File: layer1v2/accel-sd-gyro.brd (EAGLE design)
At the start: 17 parts, among them IC2 LGD20H, U1 MMA8452Q, U2 microSD

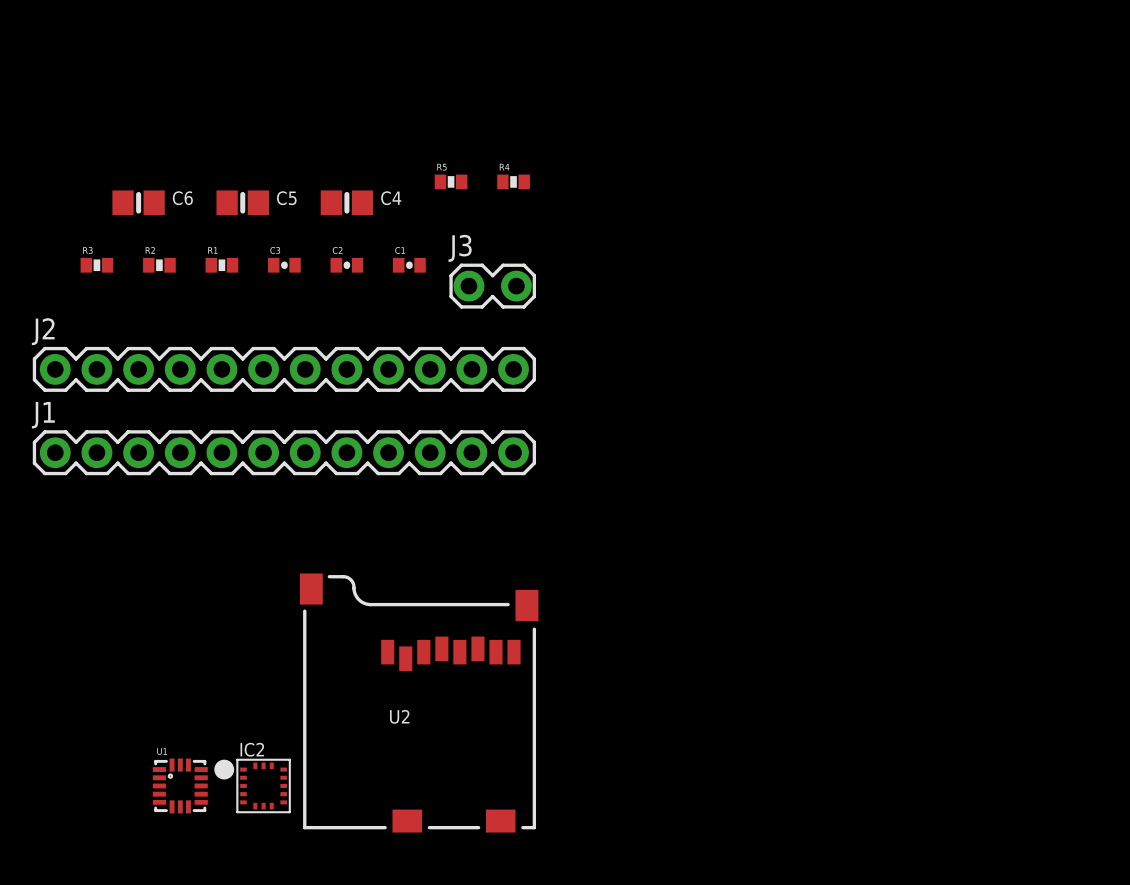
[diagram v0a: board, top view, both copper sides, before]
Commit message: created layout for just the gyro
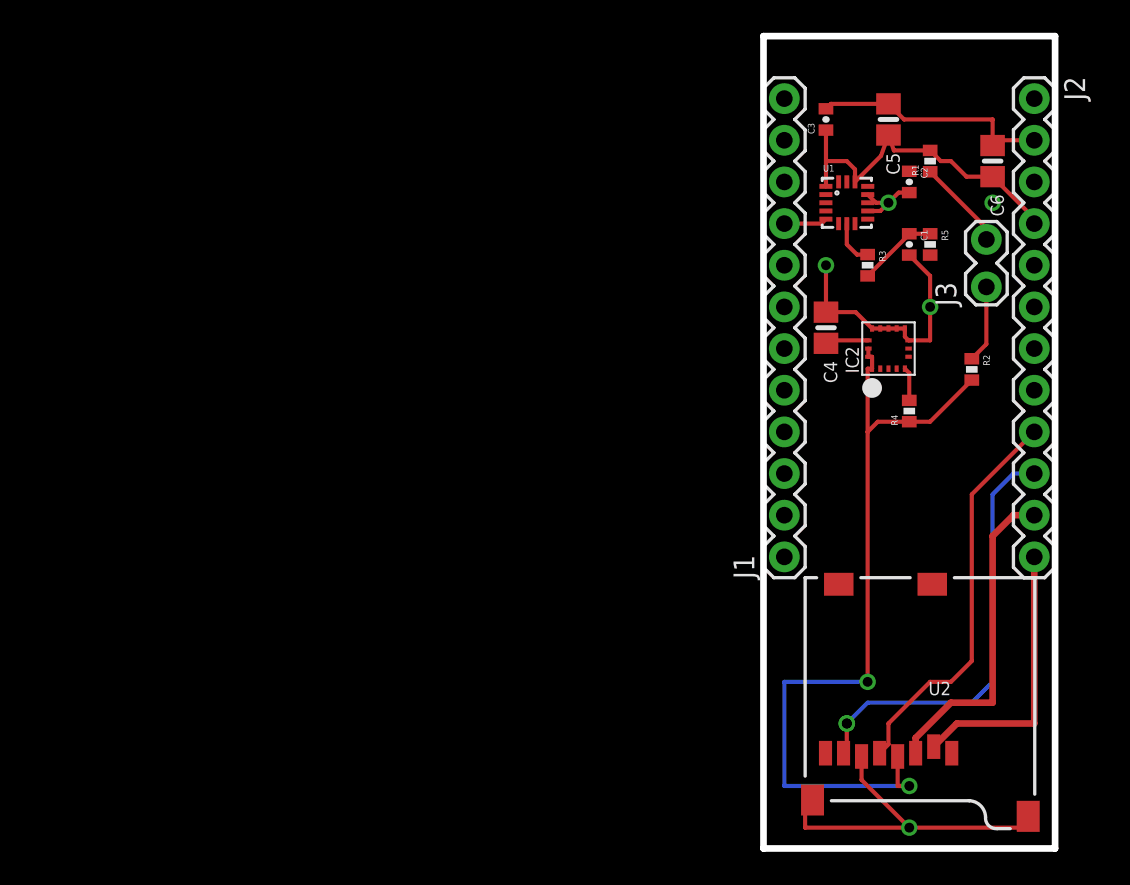
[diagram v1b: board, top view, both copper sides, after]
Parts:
- moved J2 61.9 mm to (16.5, 45.7), turned to 270 degrees
- moved U1 54.0 mm to (5.08, 39.4)
- moved C6 52.1 mm to (14.0, 41.9), turned to 270 degrees
- moved R2 49.9 mm to (12.7, 29.2), turned to 270 degrees
- moved R3 47.0 mm to (6.35, 35.6), turned to 270 degrees
- moved IC2 46.5 mm to (7.62, 30.5), turned to 90 degrees
- moved J1 44.9 mm to (1.27, 17.8), turned to 90 degrees
- moved R1 43.6 mm to (10.2, 41.9), turned to 90 degrees
- moved C5 39.7 mm to (7.62, 44.5), turned to 270 degrees
- moved C2 34.7 mm to (8.89, 40.6), turned to 270 degrees
- moved C3 34.2 mm to (3.81, 44.5), turned to 90 degrees
- moved J3 31.4 mm to (13.6, 34.4), turned to 90 degrees
- moved C1 30.5 mm to (8.89, 36.8), turned to 270 degrees
- moved C4 30.2 mm to (3.81, 31.8), turned to 270 degrees
- moved R5 29.5 mm to (10.2, 36.8), turned to 270 degrees
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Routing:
- net 3.3V: track 0.00 -> 76.3 mm, vias 0 -> 2
- net GND: track 0.00 -> 60.2 mm, vias 0 -> 3
- net MISO: track 0.00 -> 26.3 mm, vias 0 -> 1
- net SCK: track 0.00 -> 24.2 mm
- net MOSI: track 0.00 -> 19.7 mm
- net SD_CS: track 0.00 -> 16.9 mm
- net SCL: track 0.00 -> 5.55 mm
- net SDA: track 0.00 -> 4.75 mm
- net SA0: track 0.00 -> 2.79 mm
- net N$3: track 0.00 -> 2.66 mm
- net CS_3.3V: track 0.00 -> 2.05 mm
- added copper zone on layer 16, net GND
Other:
- board outline added: 17.8 x 49.5 mm

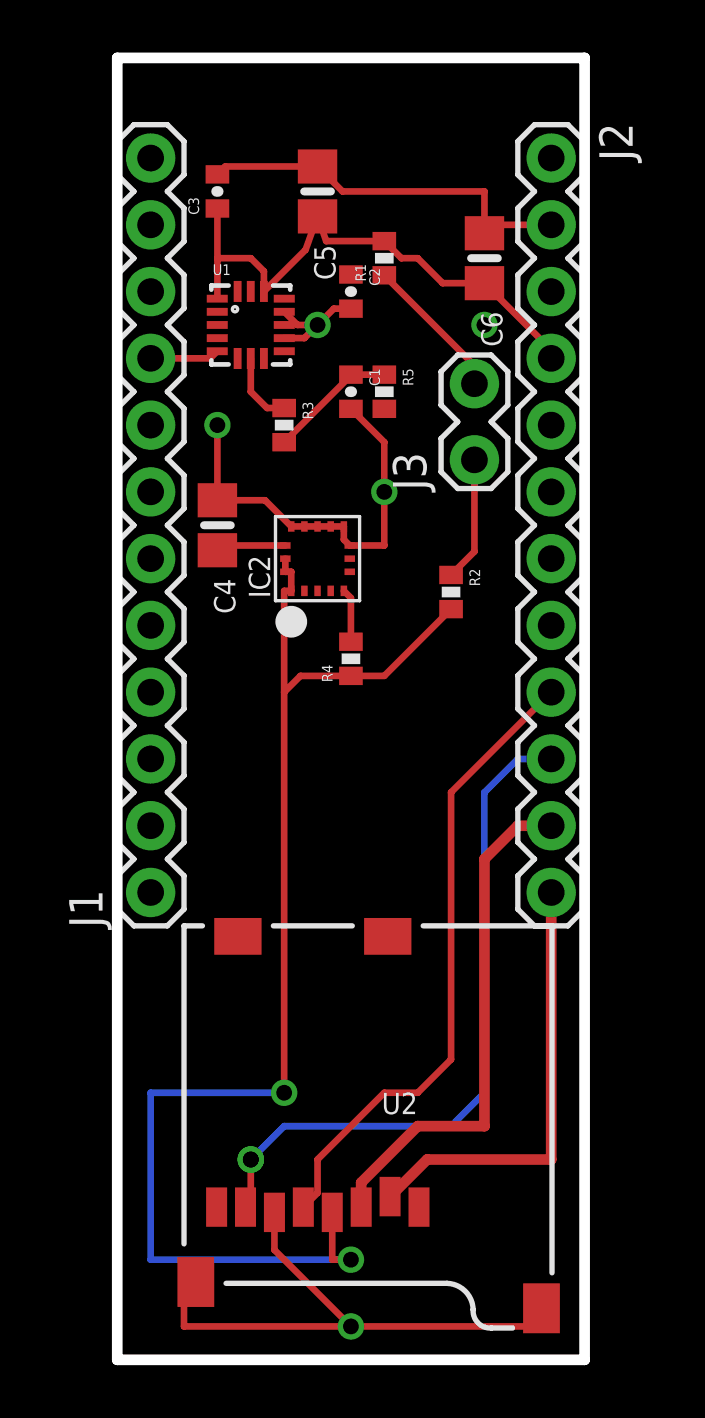
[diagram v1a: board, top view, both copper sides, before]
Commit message: intial layout of v2 board, consldated i2c resisor, added header pin row
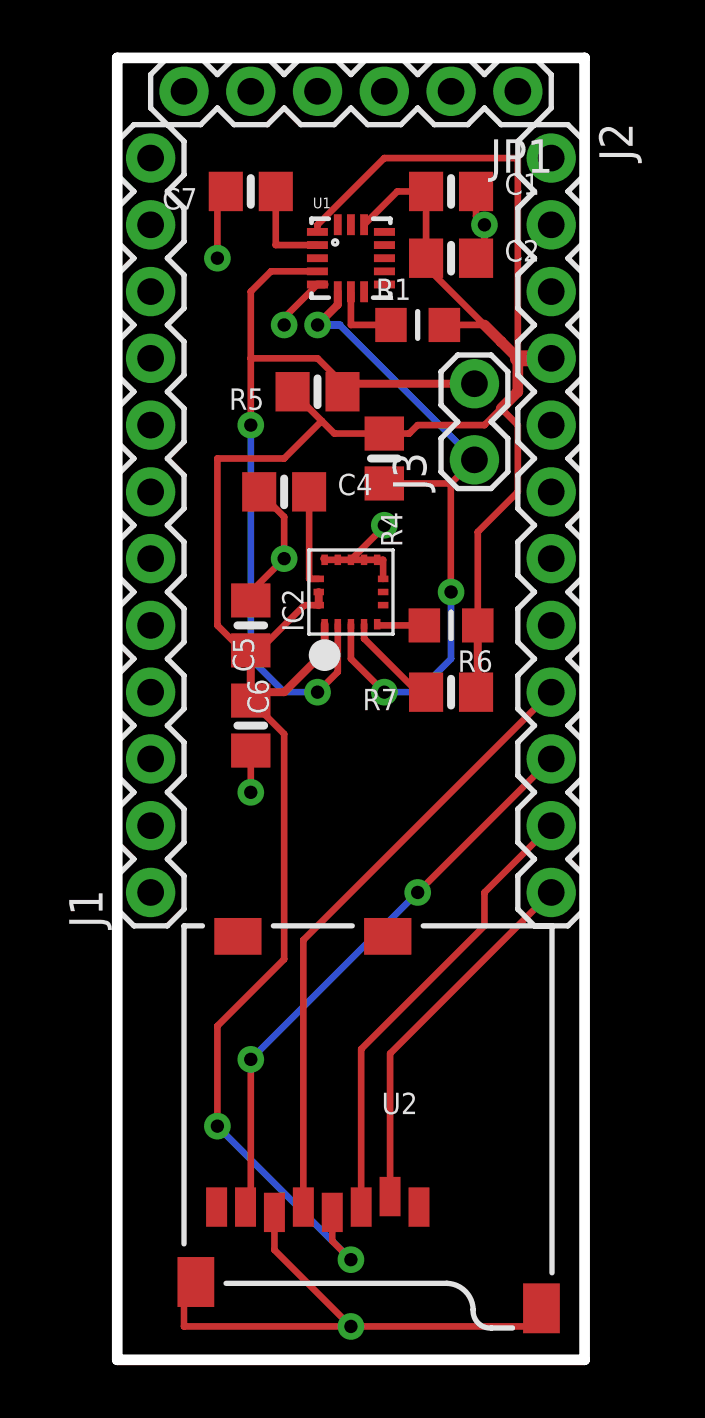
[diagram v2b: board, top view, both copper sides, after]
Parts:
- removed C3: 4.7uF, SparkFun:0402-CAP
- removed R2, R3: 10k, SparkFun:0402-RES
- added C7: 0.1uF, microbuilder:0805-NO
- added JP1: FTDI Basic, SparkFun:1X06
- added R6: 10K, microbuilder:_0805MP
- added R7: 10K, microbuilder:0805-NO
- C1: device SparkFun:0402-CAP -> microbuilder:0805-NO
- C2: value 0.1uF -> 4.7uF; device SparkFun:0402-CAP -> microbuilder:0805-NO
- R1: value 10k -> 10K; device SparkFun:0402-RES -> microbuilder:_0805MP
- R4, R5: value 10k -> 10K; device SparkFun:0402-RES -> microbuilder:0805-NO
- moved C5 20.5 mm to (5.08, 24.1), turned to 90 degrees
- moved C6 16.6 mm to (5.08, 27.9)
- moved C1 8.52 mm to (12.7, 44.5), turned to 0 degrees
- moved R4 7.73 mm to (10.2, 34.3), turned to 270 degrees
- moved U1 4.58 mm to (8.89, 41.9)
- moved C2 4.02 mm to (12.7, 41.9), turned to 0 degrees
- moved C4 2.84 mm to (6.35, 33.0), turned to 0 degrees
- moved R1 2.84 mm to (11.4, 39.4), turned to 0 degrees
- moved R5 2.54 mm to (7.62, 36.8), turned to 180 degrees
- moved IC2 1.80 mm to (8.89, 29.2)
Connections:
- removed net 3.3V: C1.1, C3.1, C5.2, C6.2, IC2.1, IC2.15, IC2.16, J2.4, R1.2, R2.2, R3.2, R4.1, R5.1, U1.1, U1.14, U2.4
- new net +3V3: C1.1, C2.1, C5.2, C6.2, IC2.1, IC2.15, IC2.16, J2.4, JP1.4, R1.2, R4.1, R5.2, R6.1, R7.1, U1.1, U1.14, U2.4
- new net DTR: JP1.1
- new net RXI: JP1.3
- new net TXO: JP1.2
- net BYP: now also C7.1; no longer C2.1
- net CS_3.3V: now also R6.2; no longer R4.2
- net GND: now also C7.2, JP1.5, JP1.6; no longer C3.2
- net SA0: now also R1.1; no longer R3.1
- net SCL: now also R5.1; no longer R1.1
- net SDA: now also R4.2; no longer R2.1
- net SDO/SAO: now also R7.2; no longer R5.2
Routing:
- net +3V3: track 0.00 -> 104.0 mm, vias 0 -> 2
- net 3.3V: track 76.3 -> 0.00 mm, vias 2 -> 0
- net SCL: track 5.55 -> 32.6 mm, vias 0 -> 2
- net SDA: track 4.75 -> 26.3 mm, vias 0 -> 3
- net GND: track 60.2 -> 41.5 mm, vias 3 -> 6
- net MISO: track 26.3 -> 22.0 mm, vias 1 -> 2
- net SDO/SAO: track 0.00 -> 4.20 mm
- net BYP: track 0.00 -> 3.63 mm
- net SD_CS: track 16.9 -> 14.1 mm
- net MOSI: track 19.7 -> 17.5 mm
- net N$3: track 2.66 -> 3.68 mm
- net SCK: track 24.2 -> 23.5 mm

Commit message: layer 1 tweaks and silk
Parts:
- removed JP1: FTDI Basic, SparkFun:1X06
- removed R6: 10K, microbuilder:_0805MP
- removed R7: 10K, microbuilder:0805-NO
- added R2: 10K, microbuilder:0805-NO
- added R3: 10K, microbuilder:_0805MP
- R1: device microbuilder:_0805MP -> microbuilder:0805-NO
- R4: device microbuilder:0805-NO -> microbuilder:_0805MP
- moved R5 12.0 mm to (11.4, 25.4)
- moved R4 6.84 mm to (12.7, 27.9), turned to 180 degrees
- moved R1 4.58 mm to (7.62, 36.8), turned to 180 degrees
- moved C2 1.27 mm to (14.0, 41.9), turned to 270 degrees
- moved C1 1.27 mm to (11.4, 44.5)
- renumbered C7 to C3
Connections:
- removed net DTR: JP1.1
- removed net RXI: JP1.3
- removed net TXO: JP1.2
- net +3V3: now also R2.1, R3.2, R5.1; no longer JP1.4, R5.2, R6.1, R7.1
- net CS_3.3V: now also R4.2; no longer R6.2
- net GND: no longer JP1.5, JP1.6
- net SA0: now also R3.1; no longer R1.1
- net SCL: now also R1.1; no longer R5.1
- net SDA: now also R2.2; no longer R4.2
- net SDO/SAO: now also R5.2; no longer R7.2
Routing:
- net +3V3: track 104.0 -> 113.1 mm
- net GND: track 41.5 -> 46.1 mm, vias 6 -> 8
- net SDO/SAO: track 4.20 -> 3.04 mm
- net SDA: track 26.3 -> 27.1 mm
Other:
- board text added: "10"
- board text added: "11"
- board text added: "12"
- board text added: "13"
- board text added: "2"
- board text added: "9"
- board text added: "GND"
- board text added: "Laney"
- board text added: "Layer 1"
- board text added: "RAW"
- board text added: "SCL"
- board text added: "SDA"
- board text added: "Sharkduino V1"
- board text added: "VCC"
- board text added: "VIMS"
- board text added: "W&M Physics"
- board text added: "William"
- board text added: "X"
- board text added: "Y"
- board text added: "Z"

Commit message: begun layer 2 desgine
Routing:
- net +3V3: track 113.1 -> 113.9 mm
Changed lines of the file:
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@@
 <setting verticaltext="up"/>
 </settings>
-<grid distance="0.05" unitdist="inch" unit="inch" style="lines" multiple="1" display="yes" altdistance="0.025" altunitdist="inch" altunit="inch"/>
+<grid distance="0.05" unitdist="inch" unit="inch" style="lines" multiple="1" display="yes" altdistance="0.005" altunitdist="inch" altunit="inch"/>
 <layers>
 <layer number="1" name="Top" color="4" fill="1" visible="yes" active="yes"/>
@@
 <layer number="25" name="tNames" color="7" fill="1" visible="no" active="yes"/>
 <layer number="26" name="bNames" color="7" fill="1" visible="no" active="yes"/>
-<layer number="27" name="tValues" color="7" fill="1" visible="yes" active="yes"/>
+<layer number="27" name="tValues" color="7" fill="1" visible="no" active="yes"/>
 <layer number="28" name="bValues" color="7" fill="1" visible="no" active="yes"/>
 <layer number="29" name="tStop" color="7" fill="3" visible="no" active="yes"/>
@@
 <wire x1="9.39" y1="43.36" x2="10.48" y2="44.45" width="0.254" layer="1"/>
 <wire x1="13.97" y1="39.37" x2="15.24" y2="38.1" width="0.254" layer="1"/>
-<wire x1="3.81" y1="8.89" x2="3.81" y2="12.7" width="0.3048" layer="1"/>
-<wire x1="3.81" y1="12.7" x2="6.35" y2="15.24" width="0.3048" layer="1"/>
-<wire x1="6.35" y1="15.24" x2="6.35" y2="17.78" width="0.3048" layer="1"/>
-<wire x1="6.35" y1="17.78" x2="12.7" y2="24.13" width="0.3048" layer="1"/>
-<wire x1="12.7" y1="24.13" x2="13.97" y2="24.13" width="0.3048" layer="1"/>
-<wire x1="13.97" y1="24.13" x2="15.24" y2="25.4" width="0.3048" layer="1"/>
 <wire x1="15.24" y1="25.4" x2="15.24" y2="29.21" width="0.3048" layer="1"/>
 <wire x1="15.24" y1="29.21" x2="13.716" y2="29.21" width="0.3048" layer="1"/>
 <wire x1="12.38" y1="25.4" x2="13.65" y2="25.4" width="0.3048" layer="1"/>
 <wire x1="13.65" y1="25.4" x2="13.716" y2="25.466" width="0.3048" layer="1"/>
+<wire x1="15.24" y1="25.4" x2="6.35" y2="16.51" width="0.3048" layer="1"/>
+<wire x1="6.35" y1="16.51" x2="6.35" y2="13.97" width="0.3048" layer="1"/>
+<wire x1="6.35" y1="13.97" x2="3.81" y2="13.97" width="0.3048" layer="1"/>
+<wire x1="3.81" y1="13.97" x2="3.81" y2="8.89" width="0.3048" layer="1"/>
 </signal>
 <signal name="CS_3.3V">
